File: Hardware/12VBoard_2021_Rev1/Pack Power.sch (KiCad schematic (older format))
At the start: 11 parts

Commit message: fixed some stuffs
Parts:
- C1, C2: renamed from C?; footprint (none) -> Capacitor_SMD:C_0603_1608Metric_Pad1.05x0.95mm_HandSolder
- Conn1: footprint (none) -> MRDT_Connectors:Anderson_2_Horizontal_Stacked
- Conn1: renamed from Conn?; footprint (none) -> MRDT_Connectors:Anderson_2_Horizontal_Stacked
- D1, D2, D3: renamed from D?; footprint (none) -> Diode_SMD:D_0603_1608Metric_Pad1.05x0.95mm_HandSolder
- R1, R2: renamed from R?; footprint (none) -> Resistor_SMD:R_0603_1608Metric_Pad1.05x0.95mm_HandSolder
- gave numbers to parts that had none: 2
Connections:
- net PackVoltage: now also D2.2 (A)
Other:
- moved on the sheet: C1, C2, Conn1A, Conn1D, D1, D2, D3, L1, R2, U1

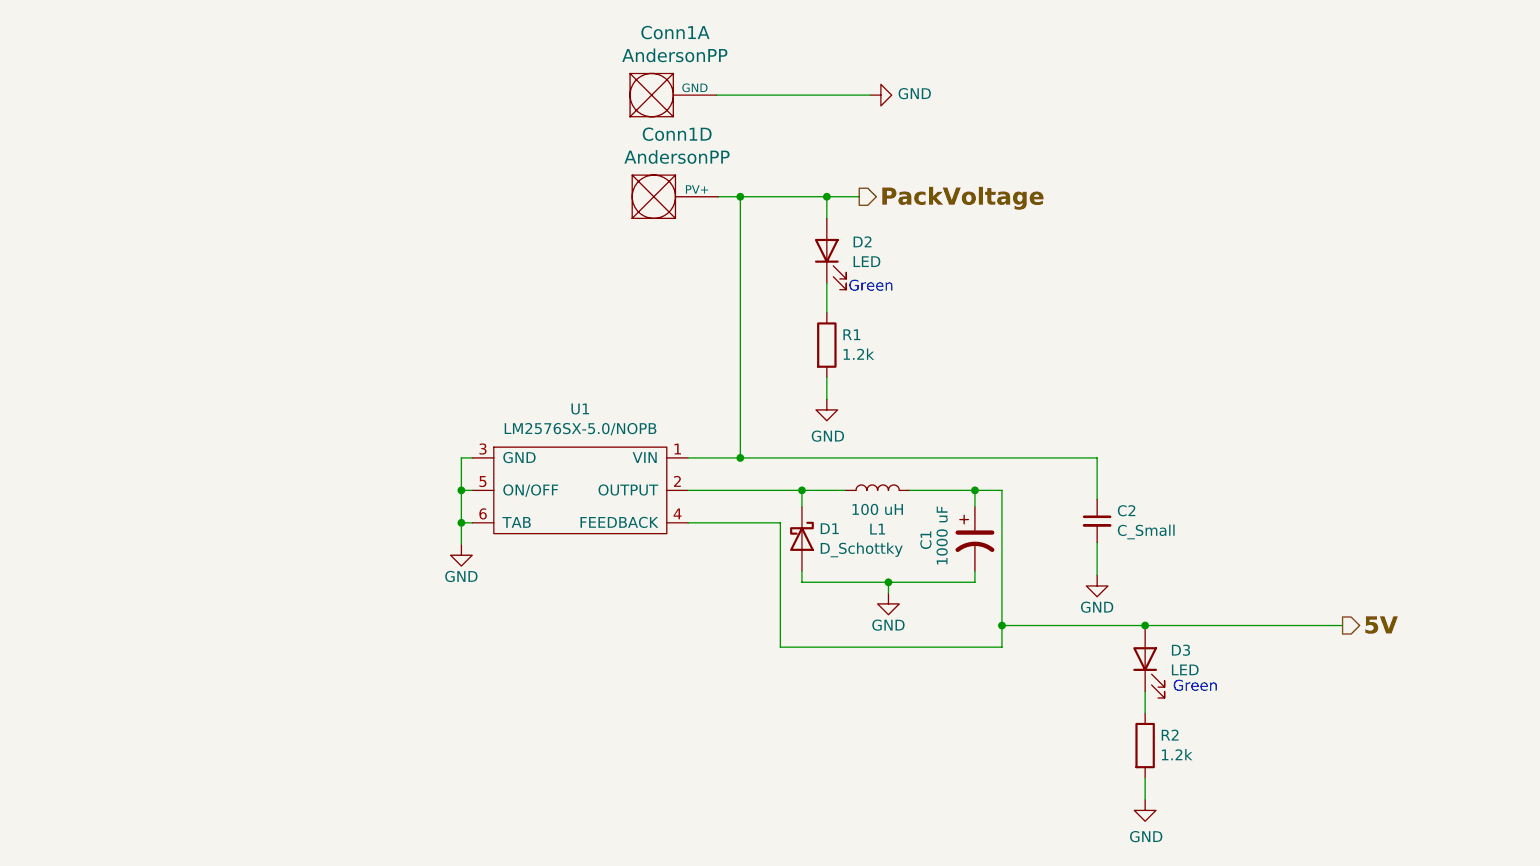
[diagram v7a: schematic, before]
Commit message: Added Component Values.
Added values to high side buck and
 footprints to components.
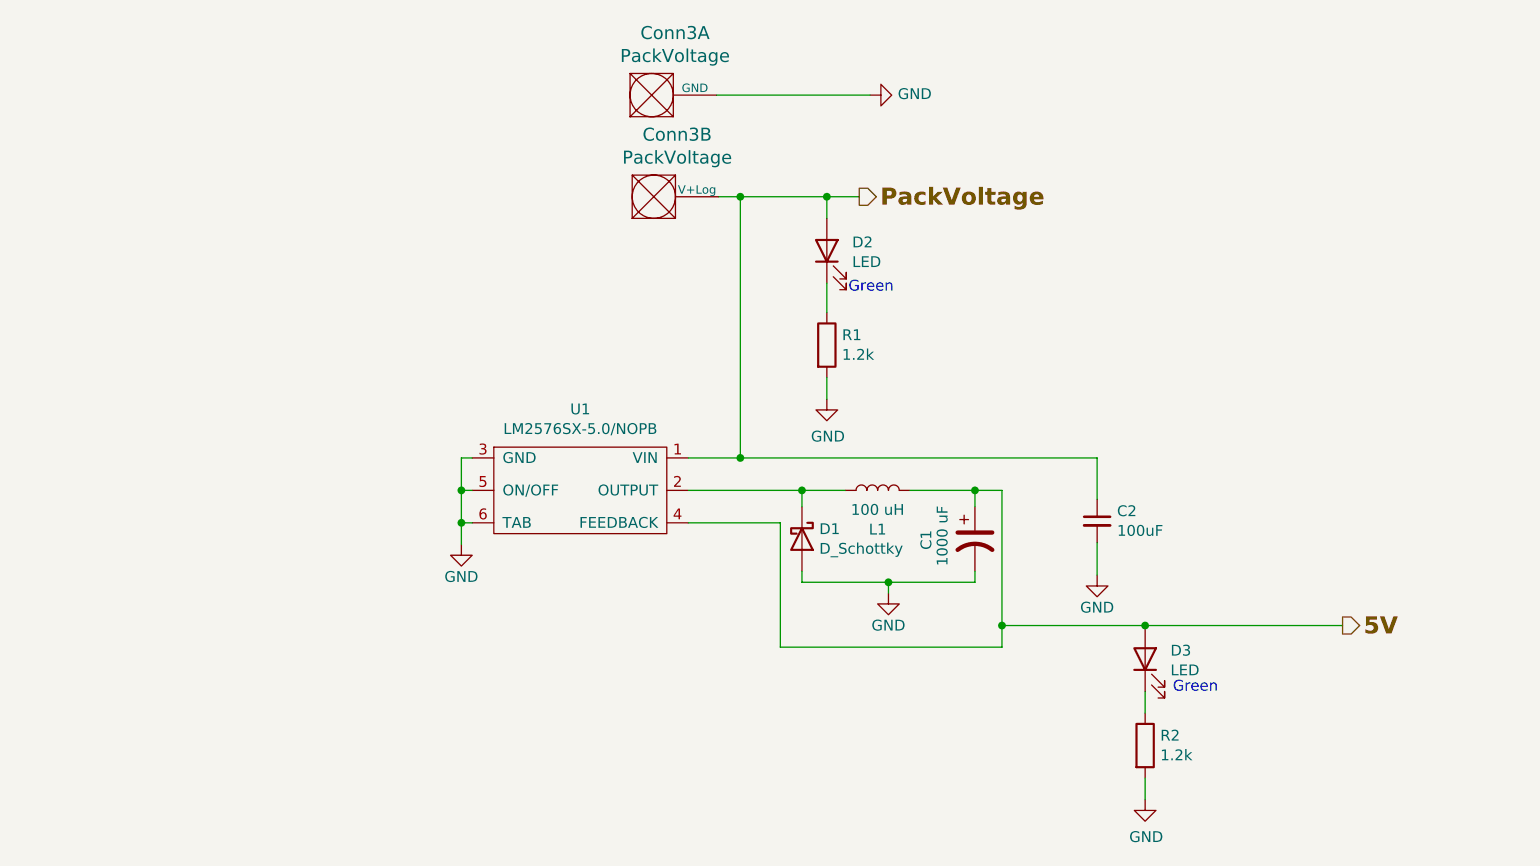
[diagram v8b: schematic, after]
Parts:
- C1: footprint Capacitor_SMD:C_0603_1608Metric_Pad1.05x0.95mm_HandSolder -> Capacitor_THT:CP_Axial_L20.0mm_D10.0mm_P26.00mm_Horizontal
- C2: value C_Small -> 100uF
- Conn3: renamed from Conn1; value AndersonPP -> PackVoltage
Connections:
- net PackVoltage: now also Conn3.2 (V+Log); no longer Conn3.4 (PV+)
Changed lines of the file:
@@
 AR Path="/5F74F223/5F7D14F6/5F8AC7A9" Ref="#PWR?"  Part="1"
 AR Path="/5F74F223/5F8AC7A9" Ref="#PWR?"  Part="1"
-AR Path="/5F8031F1/5F8AC7A9" Ref="#PWR0101"  Part="1"
-F 0 "#PWR0101" H 4160 4308 50  0001 C CNN
+AR Path="/5F8031F1/5F8AC7A9" Ref="#PWR01"  Part="1"
+F 0 "#PWR01" H 4160 4308 50  0001 C CNN
 F 1 "GND" H 4160 4408 50  0000 C CNN
 F 2 "" H 4160 4558 50  0001 C CNN
@@
 AR Path="/5F74F223/5F7D14F6/5F8A9EFD" Ref="#PWR?"  Part="1"
 AR Path="/5F74F223/5F8A9EFD" Ref="#PWR?"  Part="1"
-AR Path="/5F8031F1/5F8A9EFD" Ref="#PWR0102"  Part="1"
-F 0 "#PWR0102" H 6135 4533 50  0001 C CNN
+AR Path="/5F8031F1/5F8A9EFD" Ref="#PWR04"  Part="1"
+F 0 "#PWR04" H 6135 4533 50  0001 C CNN
 F 1 "GND" H 6135 4633 50  0000 C CNN
 F 2 "" H 6135 4783 50  0001 C CNN
@@
 F 0 "C1" V 6310 4483 50  0000 L CNN
 F 1 "1000 uF" V 6385 4408 50  0000 L CNN
-F 2 "Capacitor_SMD:C_0603_1608Metric_Pad1.05x0.95mm_HandSolder" H 6535 4533 50  0001 C CNN
+F 2 "Capacitor_THT:CP_Axial_L20.0mm_D10.0mm_P26.00mm_Horizontal" H 6535 4533 50  0001 C CNN
 F 3 "~" H 6535 4533 50  0001 C CNN
 	1    6535 4533
@@
 AR Path="/5F74F36B/5F821EB2/5F9524D7" Ref="#PWR?"  Part="1"
 AR Path="/5F74F36B/5F8236F9/5F9524D7" Ref="#PWR?"  Part="1"
-AR Path="/5F8031F1/5F9524D7" Ref="#PWR0103"  Part="1"
-F 0 "#PWR0103" H 5850 3636 50  0001 C CNN
+AR Path="/5F8031F1/5F9524D7" Ref="#PWR02"  Part="1"
+F 0 "#PWR02" H 5850 3636 50  0001 C CNN
 F 1 "GND" H 5855 3713 50  0000 C CNN
 F 2 "" H 5850 3886 50  0001 C CNN
@@
 	5850 3886 5850 3786
 $Comp
-L MRDT_Connectors:AndersonPP Conn1
-U 4 1 5F8CAA91
+L MRDT_Connectors:AndersonPP Conn3
+U 2 1 5F8CAA91
 P 4950 3050
-F 0 "Conn1" H 5158 3437 60  0000 C CNN
-F 1 "AndersonPP" H 5158 3331 60  0000 C CNN
+F 0 "Conn3" H 5158 3437 60  0000 C CNN
+F 1 "PackVoltage" H 5158 3331 60  0000 C CNN
 F 2 "MRDT_Connectors:Anderson_2_Horizontal_Stacked" H 4800 2500 60  0001 C CNN
 F 3 "" H 4800 2500 60  0001 C CNN
-	4    4950 3050
-	1    0    0    -1
-$EndComp
-$Comp
-L power:GND #PWR01
+	2    4950 3050
+	1    0    0    -1
+$EndComp
+$Comp
+L power:GND #PWR03
 U 1 1 5F804C26
 P 6050 2480
-F 0 "#PWR01" H 6050 2230 50  0001 C CNN
+F 0 "#PWR03" H 6050 2230 50  0001 C CNN
 F 1 "GND" V 6055 2352 50  0000 R CNN
 F 2 "" H 6050 2480 50  0001 C CNN
@@
 $EndComp
 $Comp
-L MRDT_Connectors:AndersonPP Conn1
+L MRDT_Connectors:AndersonPP Conn3
 U 1 1 5F803341
 P 4940 2580
-F 0 "Conn1" H 5148 2967 60  0000 C CNN
-F 1 "AndersonPP" H 5148 2861 60  0000 C CNN
+F 0 "Conn3" H 5148 2967 60  0000 C CNN
+F 1 "PackVoltage" H 5148 2861 60  0000 C CNN
 F 2 "MRDT_Connectors:Anderson_2_Horizontal_Stacked" H 4790 2030 60  0001 C CNN
 F 3 "" H 4790 2030 60  0001 C CNN
@@
 AR Path="/5F74F36B/5F821EB2/5F96E7EE" Ref="#PWR?"  Part="1"
 AR Path="/5F74F36B/5F8236F9/5F96E7EE" Ref="#PWR?"  Part="1"
-AR Path="/5F8031F1/5F96E7EE" Ref="#PWR0104"  Part="1"
-F 0 "#PWR0104" H 7322 5488 50  0001 C CNN
+AR Path="/5F8031F1/5F96E7EE" Ref="#PWR06"  Part="1"
+F 0 "#PWR06" H 7322 5488 50  0001 C CNN
 F 1 "GND" H 7327 5565 50  0000 C CNN
 F 2 "" H 7322 5738 50  0001 C CNN
@@
 P 7100 4450
 F 0 "C2" H 7192 4496 50  0000 L CNN
-F 1 "C_Small" H 7192 4405 50  0000 L CNN
+F 1 "100uF" H 7192 4405 50  0000 L CNN
 F 2 "Capacitor_SMD:C_0603_1608Metric_Pad1.05x0.95mm_HandSolder" H 7100 4450 50  0001 C CNN
 F 3 "~" H 7100 4450 50  0001 C CNN
@@
 AR Path="/5F74F223/5F7D14F6/5F982B1C" Ref="#PWR?"  Part="1"
 AR Path="/5F74F223/5F982B1C" Ref="#PWR?"  Part="1"
-AR Path="/5F8031F1/5F982B1C" Ref="#PWR0105"  Part="1"
-F 0 "#PWR0105" H 7100 4450 50  0001 C CNN
+AR Path="/5F8031F1/5F982B1C" Ref="#PWR05"  Part="1"
+F 0 "#PWR05" H 7100 4450 50  0001 C CNN
 F 1 "GND" H 7100 4550 50  0000 C CNN
 F 2 "" H 7100 4700 50  0001 C CNN
